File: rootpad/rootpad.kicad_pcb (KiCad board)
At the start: 2 copper layers, 52 parts, among them J1 USB_B_Mini, SW1 SW_Push, U1 ATmega32U4-AU, Y1 16MHz

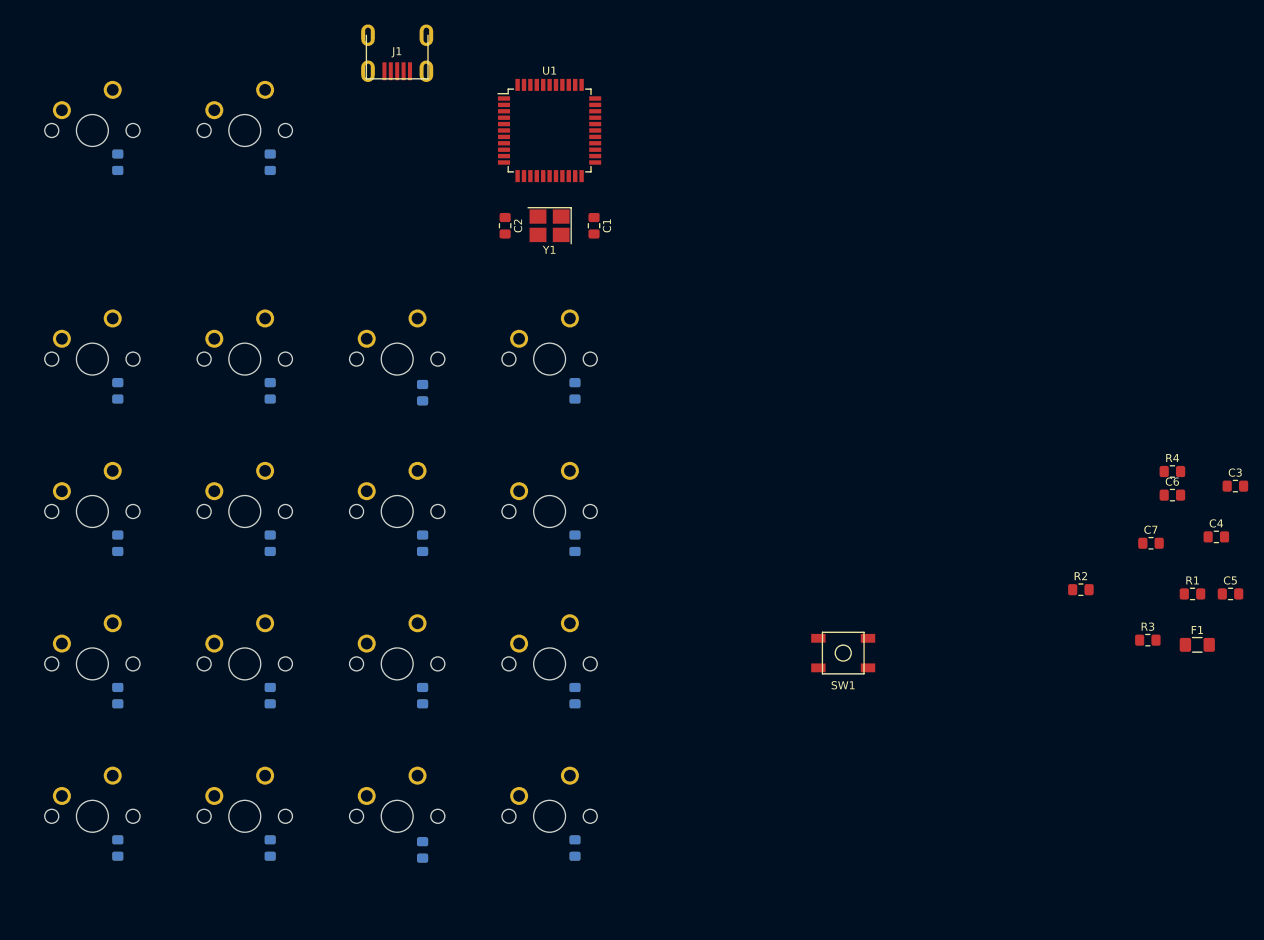
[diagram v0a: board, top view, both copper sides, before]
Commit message: Placed MCU and caps around it
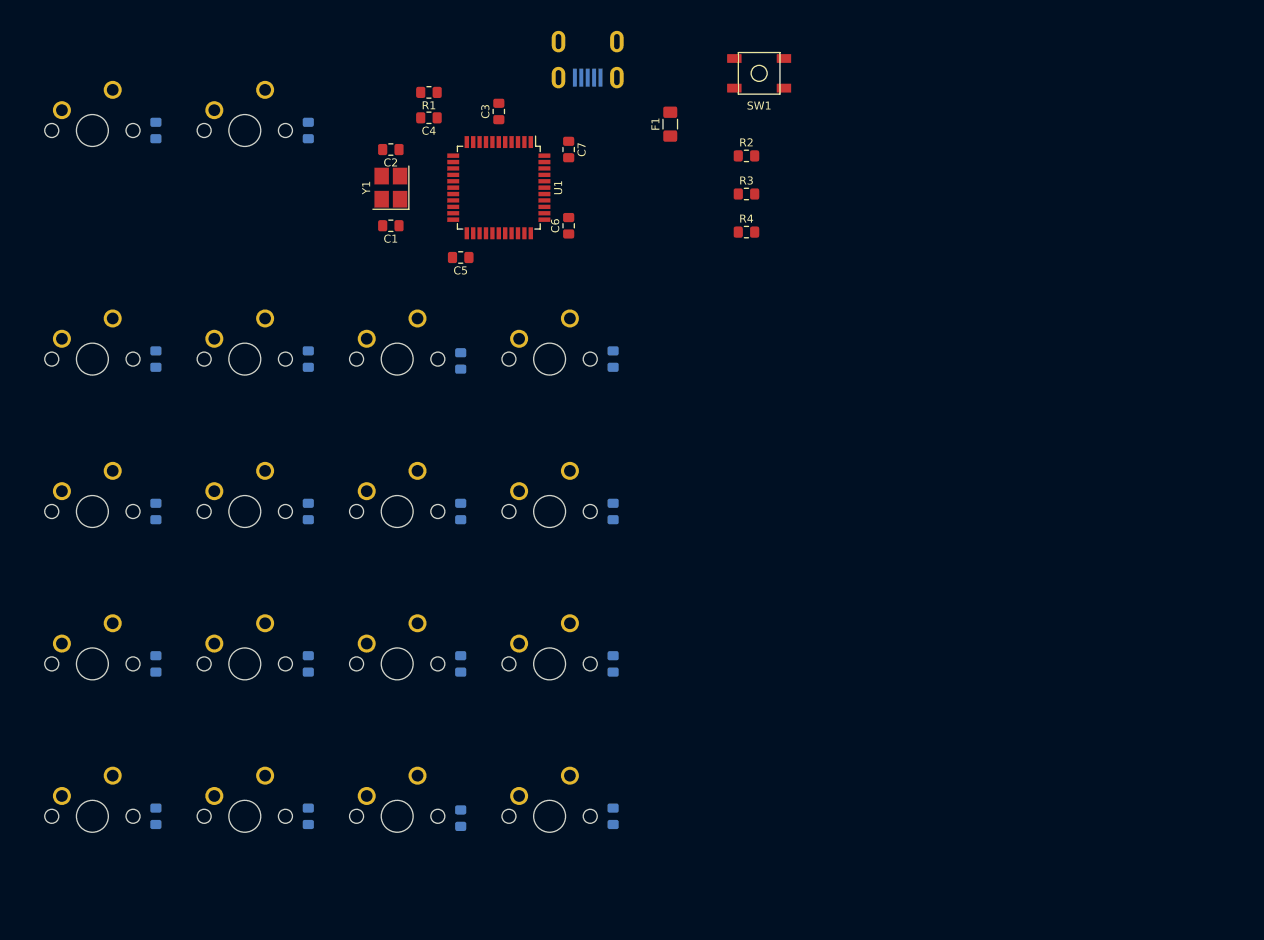
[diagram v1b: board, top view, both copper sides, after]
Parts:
- J1: moved to B.Cu
- moved R1 114.2 mm to (170.7, 52.4), turned to 180 degrees
- moved C4 111.5 mm to (170.7, 55.6), turned to 180 degrees
- moved C5 105.0 mm to (174.6, 73.0), turned to 180 degrees
- moved C3 103.3 mm to (179.4, 54.8), turned to 90 degrees
- moved F1 92.6 mm to (200.8, 56.4), turned to 90 degrees
- moved C7 87.9 mm to (188.1, 59.5), turned to 270 degrees
- moved C6 82.6 mm to (188.1, 69.1), turned to 90 degrees
- moved R3 75.0 mm to (210.3, 65.1)
- moved SW1 73.2 mm to (211.9, 50.0)
- moved R2 68.5 mm to (210.3, 60.3)
- moved R4 61.1 mm to (210.3, 69.8)
- moved C1 25.4 mm to (165.9, 69.1), turned to 180 degrees
- moved J1 23.8 mm to (190.5, 46.0)
- moved Y1 20.4 mm to (165.9, 64.3), turned to 90 degrees
- moved C2 17.2 mm to (165.9, 59.5), turned to 180 degrees
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
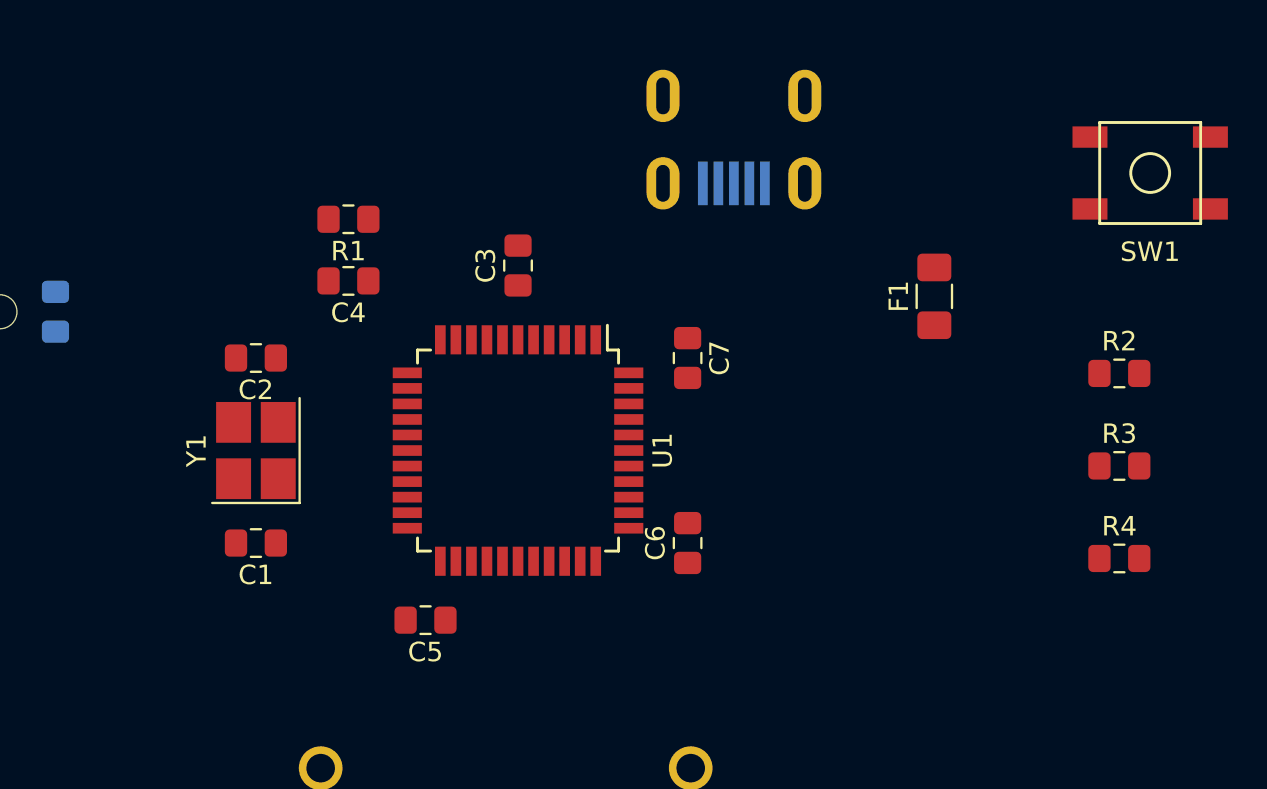
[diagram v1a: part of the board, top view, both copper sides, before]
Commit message: Initial placement of all components
Starting Routing
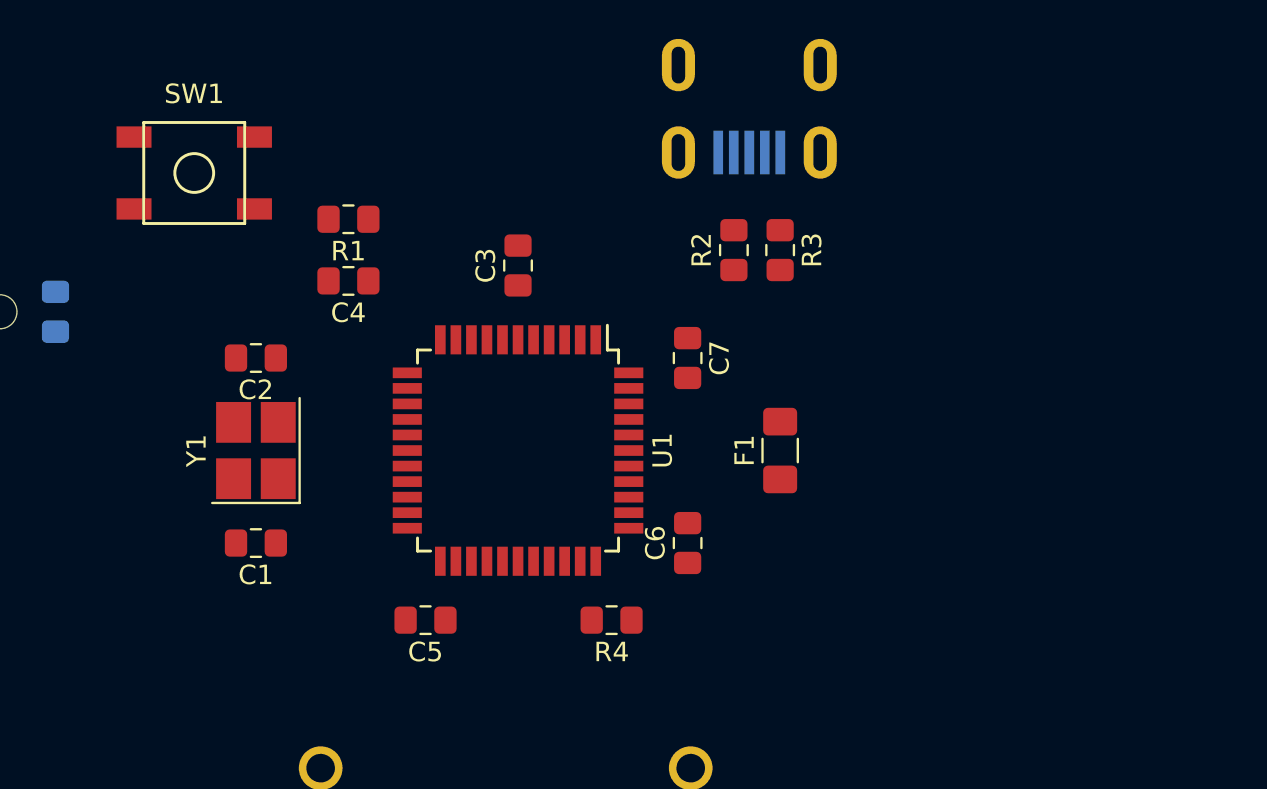
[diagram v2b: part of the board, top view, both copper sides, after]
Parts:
- moved SW1 49.2 mm to (162.7, 50.0), turned to 180 degrees
- moved R4 26.3 mm to (184.2, 73.0), turned to 180 degrees
- moved R2 20.8 mm to (190.5, 54.0), turned to 90 degrees
- moved R3 20.7 mm to (192.9, 54.0), turned to 270 degrees
- moved F1 11.2 mm to (192.9, 64.3)
- moved J1 1.77 mm to (191.3, 44.5)
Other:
- net class Default: trace_width 0.25 -> 0.254
- net class Power added: clearance 0.2, trace_width 0.381, via_dia 0.8, via_drill 0.4
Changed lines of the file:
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@@
   )
   (setup
-    (last_trace_width 0.25)
+    (last_trace_width 0.254)
     (trace_clearance 0.2)
     (zone_clearance 0.508)
@@
     (solder_mask_min_width 0.25)
     (aux_axis_origin 0 0)
-    (visible_elements FFFFF77F)
+    (visible_elements 7FFFF7FF)
     (pcbplotparams
       (layerselection 0x010fc_ffffffff)
@@
   (net_class Default "This is the default net class."
     (clearance 0.2)
-    (trace_width 0.25)
+    (trace_width 0.254)
     (via_dia 0.8)
     (via_drill 0.4)
     (uvia_dia 0.3)
     (uvia_drill 0.1)
-    (add_net +5V)
     (add_net COL0)
     (add_net COL1)
@@
     (add_net D+)
     (add_net D-)
-    (add_net GND)
     (add_net "Net-(C1-Pad1)")
     (add_net "Net-(C2-Pad2)")
@@
     (add_net ROW3)
     (add_net ROW4)
+  )
+  (net_class Power ""
+    (clearance 0.2)
+    (trace_width 0.381)
+    (via_dia 0.8)
+    (via_drill 0.4)
+    (uvia_dia 0.3)
+    (uvia_drill 0.1)
+    (add_net +5V)
+    (add_net GND)
     (add_net VCC)
   )
@@
   )
   (module random-keyboard-parts:SKQG-1155865 (layer F.Cu)
-    (at 211.93125 50.00625)
+    (at 162.71875 50.00625 180)
     (attr smd)
     (fp_text reference SW1 (at 0 4.064) (layer F.SilkS)
@@
     (fp_line (start 2.6 1.1) (end 1.1 2.6) (layer F.Fab) (width 0.15))
     (fp_line (start -2.6 1.1) (end -1.1 2.6) (layer F.Fab) (width 0.15))
-    (pad 4 smd rect (at -3.1 1.85) (size 1.8 1.1) (layers F.Cu F.Paste F.Mask))
-    (pad 3 smd rect (at 3.1 -1.85) (size 1.8 1.1) (layers F.Cu F.Paste F.Mask))
-    (pad 2 smd rect (at -3.1 -1.85) (size 1.8 1.1) (layers F.Cu F.Paste F.Mask)
+    (pad 4 smd rect (at -3.1 1.85 180) (size 1.8 1.1) (layers F.Cu F.Paste F.Mask))
+    (pad 3 smd rect (at 3.1 -1.85 180) (size 1.8 1.1) (layers F.Cu F.Paste F.Mask))
+    (pad 2 smd rect (at -3.1 -1.85 180) (size 1.8 1.1) (layers F.Cu F.Paste F.Mask)
       (net 35 "Net-(R1-Pad2)"))
-    (pad 1 smd rect (at 3.1 1.85) (size 1.8 1.1) (layers F.Cu F.Paste F.Mask)
+    (pad 1 smd rect (at 3.1 1.85 180) (size 1.8 1.1) (layers F.Cu F.Paste F.Mask)
       (net 1 GND))
   )
   (module Resistor_SMD:R_0805_2012Metric_Pad1.15x1.40mm_HandSolder (layer F.Cu)
-    (at 210.34375 69.85)
+    (at 184.2045 73.025 180)
     (descr "Resistor SMD 0805 (2012 Metric), square (rectangular) end terminal, IPC_7351 nominal with elongated pad for handsoldering. (Body size source: https://docs.google.com/spreadsheets/d/1BsfQQcO9C6DZCsRaXUlFlo91Tg2WpOkGARC1WS5S8t0/edit?usp=sharing), generated with kicad-footprint-generator")
     (tags "resistor handsolder")
@@
     (fp_line (start -1 -0.6) (end 1 -0.6) (layer F.Fab) (width 0.1))
     (fp_line (start -1 0.6) (end -1 -0.6) (layer F.Fab) (width 0.1))
-    (pad 2 smd roundrect (at 1.025 0) (size 1.15 1.4) (layers F.Cu F.Paste F.Mask) (roundrect_rratio 0.217391)
+    (pad 2 smd roundrect (at 1.025 0 180) (size 1.15 1.4) (layers F.Cu F.Paste F.Mask) (roundrect_rratio 0.217391)
       (net 39 "Net-(R4-Pad2)"))
-    (pad 1 smd roundrect (at -1.025 0) (size 1.15 1.4) (layers F.Cu F.Paste F.Mask) (roundrect_rratio 0.217391)
+    (pad 1 smd roundrect (at -1.025 0 180) (size 1.15 1.4) (layers F.Cu F.Paste F.Mask) (roundrect_rratio 0.217391)
       (net 1 GND))
     (model ${KISYS3DMOD}/Resistor_SMD.3dshapes/R_0805_2012Metric.wrl
@@
   )
   (module Resistor_SMD:R_0805_2012Metric_Pad1.15x1.40mm_HandSolder (layer F.Cu)
-    (at 210.34375 65.0875)
+    (at 192.88125 53.975 270)
     (descr "Resistor SMD 0805 (2012 Metric), square (rectangular) end terminal, IPC_7351 nominal with elongated pad for handsoldering. (Body size source: https://docs.google.com/spreadsheets/d/1BsfQQcO9C6DZCsRaXUlFlo91Tg2WpOkGARC1WS5S8t0/edit?usp=sharing), generated with kicad-footprint-generator")
     (tags "resistor handsolder")
     (attr smd)
-    (fp_text reference R3 (at 0 -1.65) (layer F.SilkS)
-      (effects (font (size 1 1) (thickness 0.15)))
-    )
-    (fp_text value 22 (at 0 1.65) (layer F.Fab)
-      (effects (font (size 1 1) (thickness 0.15)))
-    )
-    (fp_text user %R (at 0 0) (layer F.Fab)
+    (fp_text reference R3 (at 0 -1.65 90) (layer F.SilkS)
+      (effects (font (size 1 1) (thickness 0.15)))
+    )
+    (fp_text value 22 (at 0 1.65 90) (layer F.Fab)
+      (effects (font (size 1 1) (thickness 0.15)))
+    )
+    (fp_text user %R (at 0 0 90) (layer F.Fab)
       (effects (font (size 0.5 0.5) (thickness 0.08)))
     )
@@
     (fp_line (start -1 -0.6) (end 1 -0.6) (layer F.Fab) (width 0.1))
     (fp_line (start -1 0.6) (end -1 -0.6) (layer F.Fab) (width 0.1))
-    (pad 2 smd roundrect (at 1.025 0) (size 1.15 1.4) (layers F.Cu F.Paste F.Mask) (roundrect_rratio 0.217391)
+    (pad 2 smd roundrect (at 1.025 0 270) (size 1.15 1.4) (layers F.Cu F.Paste F.Mask) (roundrect_rratio 0.217391)
       (net 38 "Net-(R3-Pad2)"))
-    (pad 1 smd roundrect (at -1.025 0) (size 1.15 1.4) (layers F.Cu F.Paste F.Mask) (roundrect_rratio 0.217391)
+    (pad 1 smd roundrect (at -1.025 0 270) (size 1.15 1.4) (layers F.Cu F.Paste F.Mask) (roundrect_rratio 0.217391)
       (net 30 D-))
     (model ${KISYS3DMOD}/Resistor_SMD.3dshapes/R_0805_2012Metric.wrl
@@
   )
   (module Resistor_SMD:R_0805_2012Metric_Pad1.15x1.40mm_HandSolder (layer F.Cu)
-    (at 210.34375 60.325)
+    (at 190.5 53.975 90)
     (descr "Resistor SMD 0805 (2012 Metric), square (rectangular) end terminal, IPC_7351 nominal with elongated pad for handsoldering. (Body size source: https://docs.google.com/spreadsheets/d/1BsfQQcO9C6DZCsRaXUlFlo91Tg2WpOkGARC1WS5S8t0/edit?usp=sharing), generated with kicad-footprint-generator")
     (tags "resistor handsolder")
     (attr smd)
-    (fp_text reference R2 (at 0 -1.65) (layer F.SilkS)
-      (effects (font (size 1 1) (thickness 0.15)))
-    )
-    (fp_text value 22 (at 0 1.65) (layer F.Fab)
-      (effects (font (size 1 1) (thickness 0.15)))
-    )
-    (fp_text user %R (at 0 0) (layer F.Fab)
+    (fp_text reference R2 (at 0 -1.65 90) (layer F.SilkS)
+      (effects (font (size 1 1) (thickness 0.15)))
+    )
+    (fp_text value 22 (at 0 1.65 90) (layer F.Fab)
+      (effects (font (size 1 1) (thickness 0.15)))
+    )
+    (fp_text user %R (at 0 0 90) (layer F.Fab)
       (effects (font (size 0.5 0.5) (thickness 0.08)))
     )
@@
     (fp_line (start -1 -0.6) (end 1 -0.6) (layer F.Fab) (width 0.1))
     (fp_line (start -1 0.6) (end -1 -0.6) (layer F.Fab) (width 0.1))
-    (pad 2 smd roundrect (at 1.025 0) (size 1.15 1.4) (layers F.Cu F.Paste F.Mask) (roundrect_rratio 0.217391)
+    (pad 2 smd roundrect (at 1.025 0 90) (size 1.15 1.4) (layers F.Cu F.Paste F.Mask) (roundrect_rratio 0.217391)
       (net 36 D+))
-    (pad 1 smd roundrect (at -1.025 0) (size 1.15 1.4) (layers F.Cu F.Paste F.Mask) (roundrect_rratio 0.217391)
+    (pad 1 smd roundrect (at -1.025 0 90) (size 1.15 1.4) (layers F.Cu F.Paste F.Mask) (roundrect_rratio 0.217391)
       (net 37 "Net-(R2-Pad1)"))
     (model ${KISYS3DMOD}/Resistor_SMD.3dshapes/R_0805_2012Metric.wrl
@@
   )
   (module random-keyboard-parts:Molex-0548190589 (layer B.Cu)
-    (at 190.5 46.0375 270)
+    (at 191.29375 44.45 270)
     (attr smd)
     (fp_text reference J1 (at 2.032 0) (layer B.SilkS)
@@
   )
   (module Fuse:Fuse_1206_3216Metric_Pad1.42x1.75mm_HandSolder (layer F.Cu)
-    (at 200.81875 56.35625 90)
+    (at 192.88125 64.29375 90)
     (descr "Fuse SMD 1206 (3216 Metric), square (rectangular) end terminal, IPC_7351 nominal with elongated pad for handsoldering. (Body size source: http://www.tortai-tech.com/upload/download/2011102023233369053.pdf), generated with kicad-footprint-generator")
     (tags "resistor handsolder")

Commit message: Initial routing
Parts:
- F1, R2, R3: moved to B.Cu
- moved R2 0.79 mm to (190.5, 53.2)
- moved R3 0.79 mm to (192.9, 53.2)
- turned R1 to 0 degrees
- turned SW1 to 270 degrees
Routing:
- net GND: track 0.00 -> 128.8 mm, vias 0 -> 1
- net +5V: track 0.00 -> 32.5 mm, vias 0 -> 1
- net Net-(R1-Pad2): track 0.00 -> 23.3 mm
- net VCC: track 0.00 -> 15.3 mm
- net Net-(R3-Pad2): track 0.00 -> 14.3 mm, vias 0 -> 1
- net Net-(C2-Pad2): track 0.00 -> 13.8 mm
- net Net-(R2-Pad1): track 0.00 -> 12.7 mm, vias 0 -> 1
- net Net-(C1-Pad1): track 0.00 -> 10.6 mm
- net D+: track 0.00 -> 3.54 mm
- net D-: track 0.00 -> 3.53 mm
- net Net-(R4-Pad2): track 0.00 -> 3.12 mm
- net Net-(C3-Pad1): track 0.00 -> 2.80 mm
